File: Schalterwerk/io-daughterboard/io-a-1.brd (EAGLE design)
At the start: 100 x 80 mm, 34 parts, among them Q1 BSS123, Q2 BSS123, Q3 BSS123, Q4 BSS123, Q5 BSS123, Q6 BSS123, Q7 BSS123, Q8 BSS123, U1 74HC166, U2 74HC166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

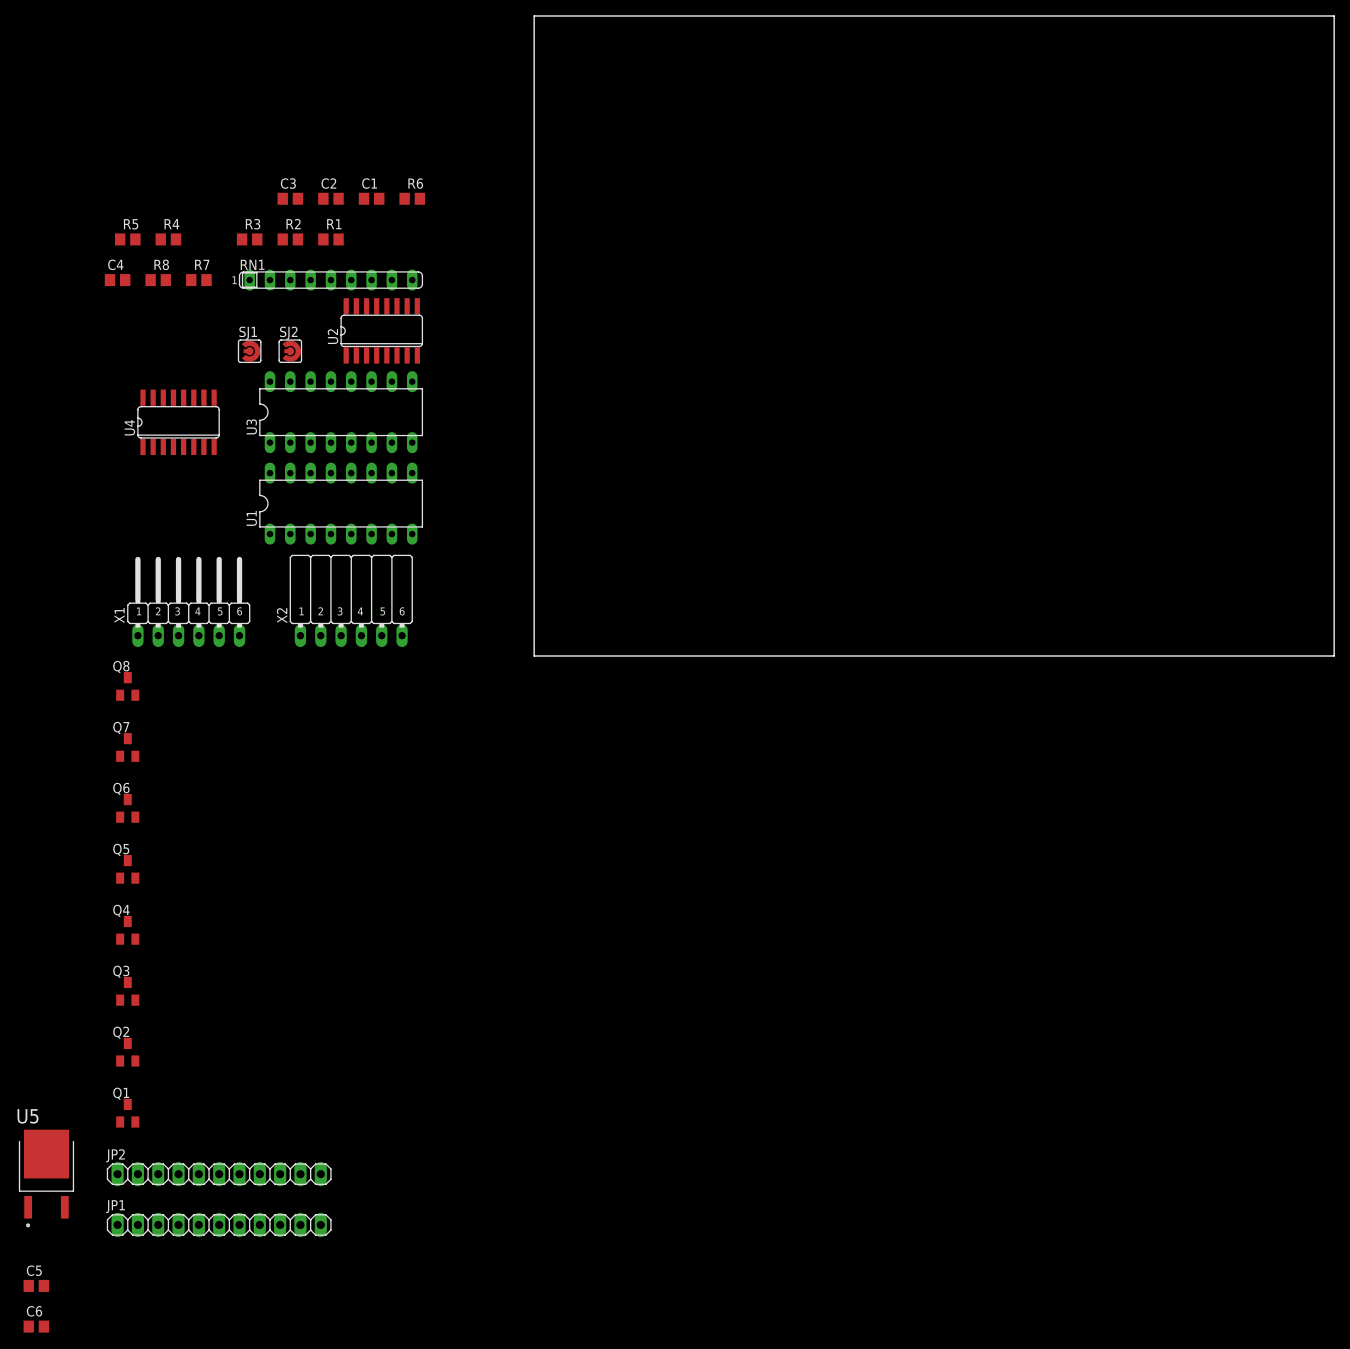
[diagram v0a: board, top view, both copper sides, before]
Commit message: Completes board layout and routing for the daughterboard.
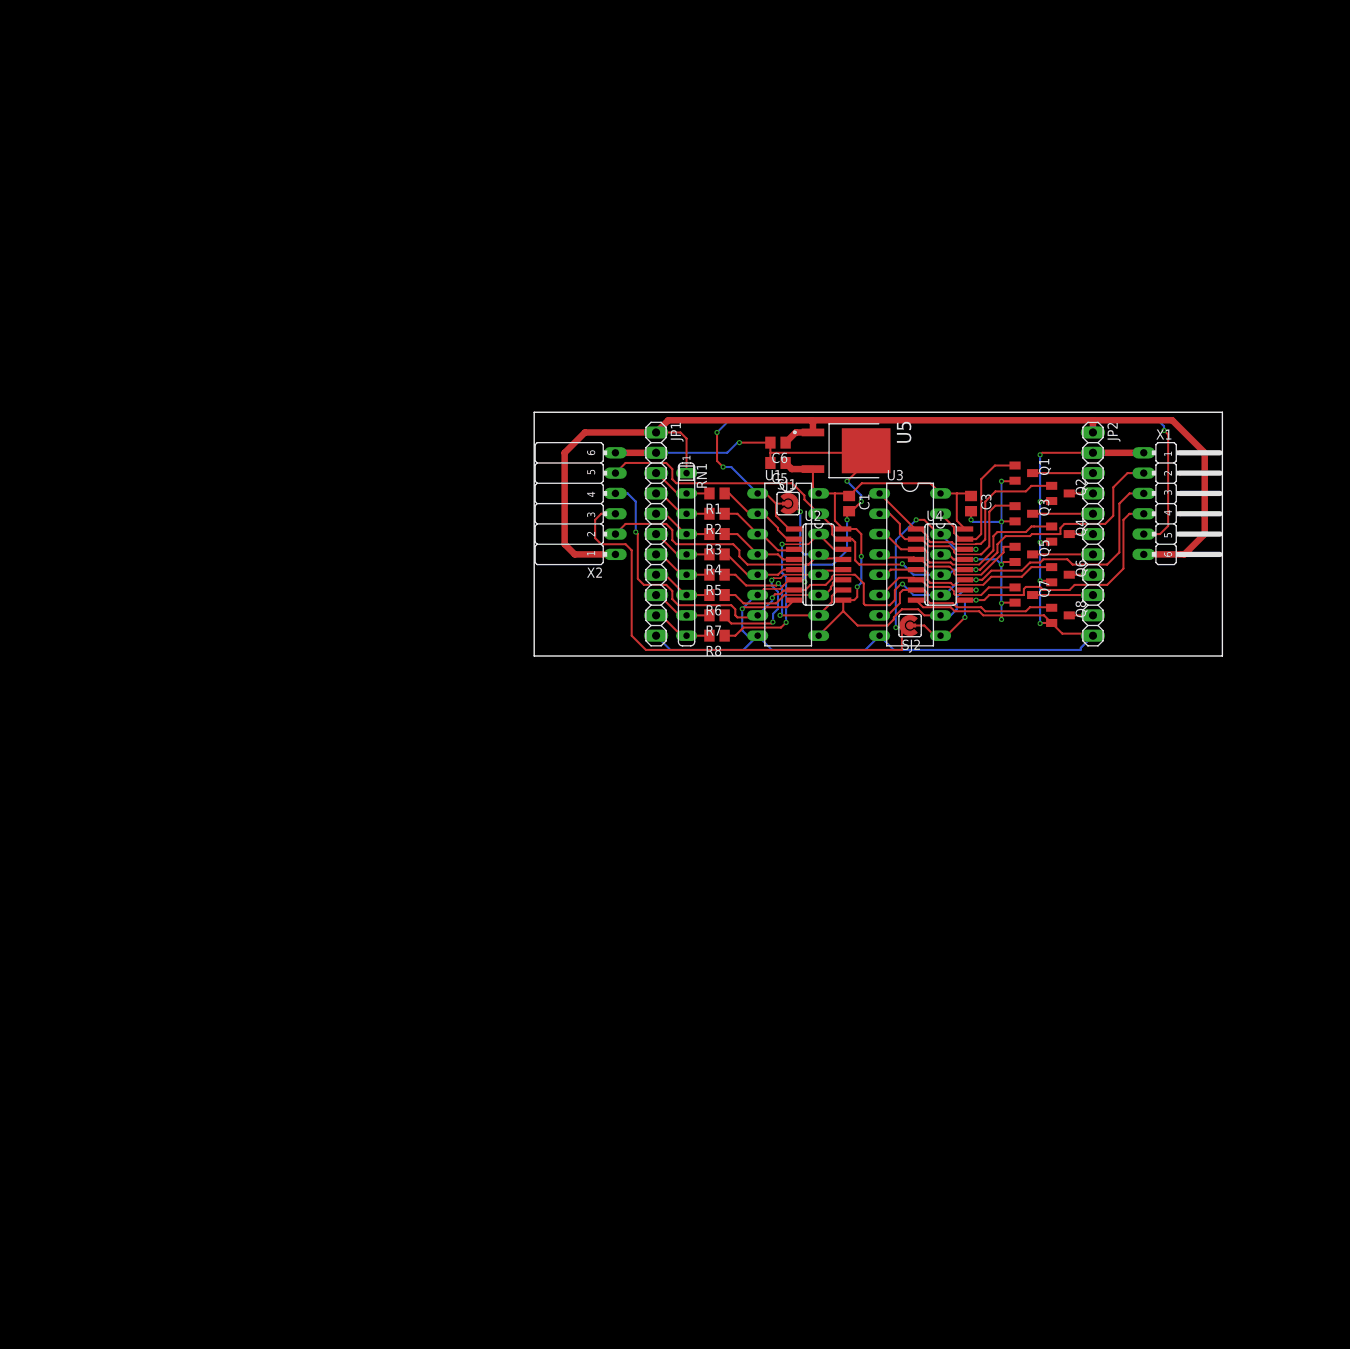
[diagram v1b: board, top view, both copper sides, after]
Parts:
- removed C2, C4: (no value), rcl:C0805
- moved C6 144.2 mm to (30.5, 26.7), turned to 180 degrees
- moved C5 138.5 mm to (30.5, 24.1), turned to 180 degrees
- moved Q1 137.7 mm to (61.2, 22.9), turned to 270 degrees
- moved Q2 135.9 mm to (65.8, 20.3), turned to 270 degrees
- moved JP2 135.4 mm to (69.8, 15.2), turned to 270 degrees
- moved U5 134.8 mm to (39.0, 25.7), turned to 270 degrees
- moved Q3 126.9 mm to (61.2, 17.8), turned to 270 degrees
- moved Q4 126.7 mm to (65.8, 15.2), turned to 270 degrees
- moved Q6 120.2 mm to (65.8, 10.2), turned to 270 degrees
- moved Q5 118.7 mm to (61.2, 12.7), turned to 270 degrees
- moved X1 117.7 mm to (76.2, 16.5), turned to 270 degrees
- moved Q8 116.9 mm to (65.8, 5.08), turned to 270 degrees
- moved Q7 113.6 mm to (61.2, 7.62), turned to 270 degrees
- moved JP1 102.2 mm to (15.2, 15.2), turned to 270 degrees
- moved U4 96.9 mm to (50.8, 11.4), turned to 270 degrees
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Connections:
- net N$1 renamed QA
- net N$11 renamed PF
- net N$12 renamed PE
- net N$14 renamed PH
- net N$15 renamed PG
- net N$17 renamed PC
- net N$2 renamed QB
- net N$23 renamed PD
- net N$3 renamed QC
- net N$39 renamed PB
- net N$4 renamed QD
- net N$41 renamed PA
- net N$5 renamed QE
- net N$6 renamed QF
- net N$7 renamed QG
- net N$8 renamed QH
- net +12V: now also X1.6; no longer X1.1
- net +5V: no longer C2.1, C4.1
- net GND: now also X1.1; no longer C2.2, C4.2, X1.6
- net LATCH: now also X1.2; no longer X1.5
- net MISO-DN: now also X1.5; no longer X1.2
- net MOSI-DN: now also X1.4; no longer X1.3
- net SCK: now also X1.3; no longer X1.4
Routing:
- net GND: track 0.00 -> 239.8 mm, vias 0 -> 18
- net +12V: track 0.00 -> 136.1 mm
- net SCK: track 0.00 -> 98.0 mm, vias 0 -> 4
- net MISO-DN: track 0.00 -> 92.0 mm, vias 0 -> 3
- net LATCH: track 0.00 -> 85.1 mm, vias 0 -> 2
- net MOSI-UP: track 0.00 -> 84.4 mm, vias 0 -> 3
- net +5V: track 0.00 -> 77.8 mm, vias 0 -> 3
- net MOSI-DN: track 0.00 -> 42.7 mm, vias 0 -> 2
- net MISO-UP: track 0.00 -> 41.6 mm, vias 0 -> 1
- net PB: track 0.00 -> 30.2 mm
- net QH: track 0.00 -> 27.3 mm, vias 0 -> 2
- net PD: track 0.00 -> 26.7 mm
- net PH: track 0.00 -> 25.5 mm
- net PC: track 0.00 -> 25.1 mm
- net PF: track 0.00 -> 24.0 mm
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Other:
- board size 100 x 80 mm -> 86 x 30.5 mm

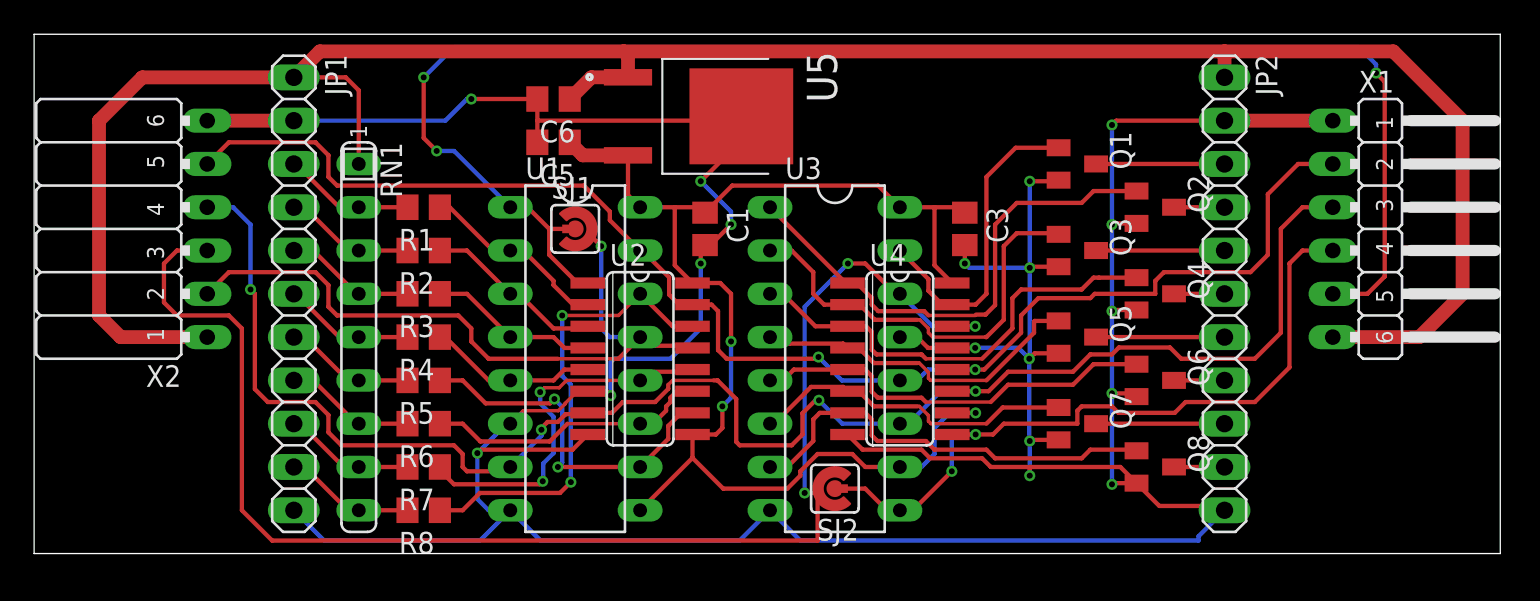
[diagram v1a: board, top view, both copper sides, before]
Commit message: Updates board size to match grid.
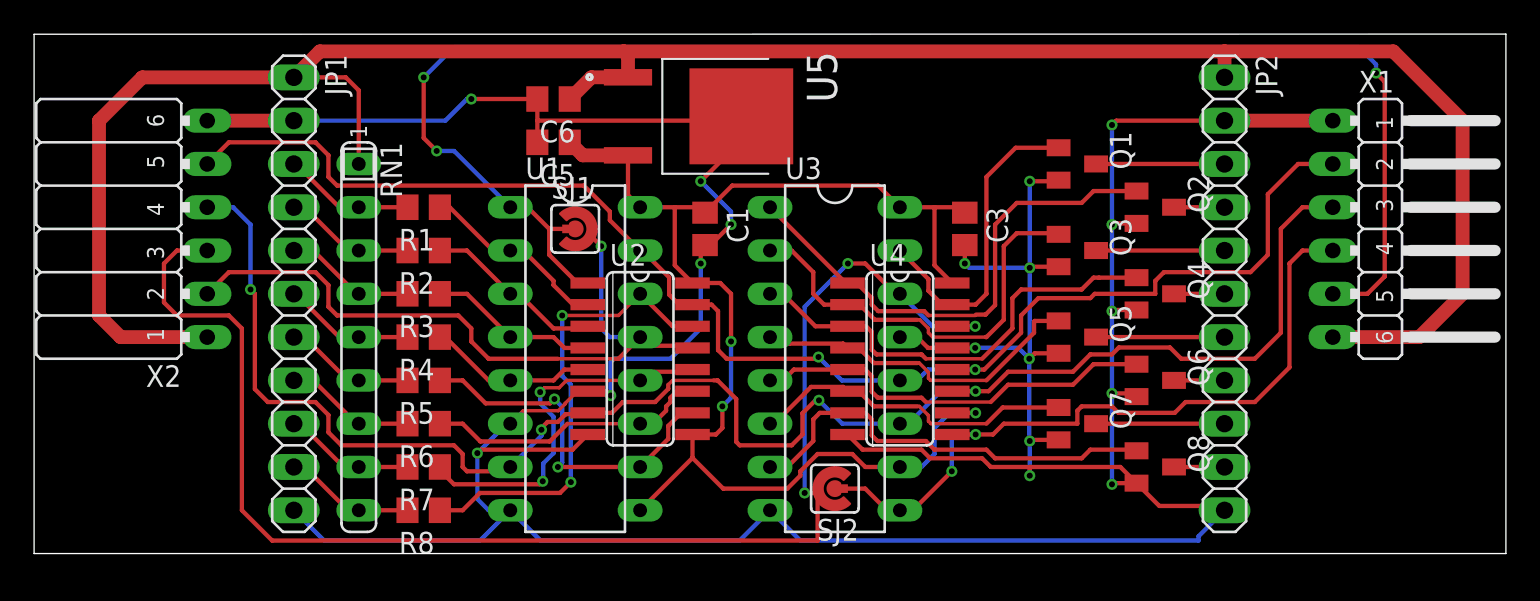
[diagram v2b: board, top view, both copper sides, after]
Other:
- board size 86 x 30.5 mm -> 86.4 x 30.5 mm
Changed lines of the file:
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@@
 <board>
 <plain>
-<wire x1="0" y1="0" x2="86.03" y2="0" width="0" layer="20"/>
-<wire x1="86.03" y1="0" x2="86.03" y2="30.47" width="0" layer="20"/>
-<wire x1="86.03" y1="30.47" x2="0" y2="30.47" width="0" layer="20"/>
+<wire x1="0" y1="0" x2="86.36" y2="0" width="0" layer="20"/>
+<wire x1="86.36" y1="0" x2="86.36" y2="30.48" width="0" layer="20"/>
+<wire x1="86.36" y1="30.48" x2="0" y2="30.47" width="0" layer="20"/>
 <wire x1="0" y1="30.47" x2="0" y2="0" width="0" layer="20"/>
 </plain>

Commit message: Adds molex picoblade connectors as alternative for uplink/dnlink.
Finishes layout with labels and text.
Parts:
- added X3, X4: MOLEX_530470610CON_530470610_MOL, eagleparts:CON_530470610_MOL
- U3, U4: value 74AHCT595N -> 74HC595
- moved X1 3.81 mm to (72.4, 16.5)
- moved X2 2.54 mm to (12.7, 21.6)
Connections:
- net +12V: now also X3.1, X4.6
- net GND: now also X3.6, X4.1
- net LATCH: now also X3.5, X4.2
- net MISO-DN: now also X4.5
- net MISO-UP: now also X3.2
- net MOSI-DN: now also X4.4
- net MOSI-UP: now also X3.3
- net SCK: now also X3.4, X4.3
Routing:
- net LATCH: track 85.1 -> 127.2 mm, vias 2 -> 6
- net SCK: track 98.0 -> 126.3 mm, vias 4 -> 9
- net GND: track 239.8 -> 254.4 mm
- net +12V: track 136.1 -> 150.4 mm
- net MOSI-DN: track 42.7 -> 55.0 mm, vias 2 -> 4
- net MISO-UP: track 41.6 -> 53.1 mm, vias 1 -> 3
- net MISO-DN: track 92.0 -> 102.4 mm, vias 3 -> 5
- net MOSI-UP: track 84.4 -> 86.3 mm, vias 3 -> 5
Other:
- board size 86.4 x 30.5 mm -> 80 x 30.5 mm
- board text added: "(c) Balazs Racz 20230522"
- board text added: "DNLINK"
- board text added: "UPLINK"
- board text added: "UPLink NUR mit DNLink verbinden!"
